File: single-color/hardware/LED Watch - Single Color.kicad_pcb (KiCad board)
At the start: 4 copper layers, 42 x 51.2 mm, 197 parts, among them J1 LiPo, J1B LiPo, J2 UPDI pogo pads 1.27 mm (RESET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, M0 LED white 0402, M1 LED white 0402, M10 LED white 0402, M11 LED white 0402, M12 LED white 0402, M13 LED white 0402, M14 LED white 0402, M15 LED white 0402, M16 LED white 0402, M17 LED white 0402, M18 LED white 0402, M19 LED white 0402, M2 LED white 0402, M20 LED white 0402, M21 LED white 0402, M22 LED white 0402, M23 LED white 0402, M24 LED white 0402, M25 LED white 0402, M26 LED white 0402, M27 LED white 0402, M28 LED white 0402, M29 LED white 0402, M3 LED white 0402, M30 LED white 0402, M31 LED white 0402, M32 LED white 0402, M33 LED white 0402, M34 LED white 0402, M35 LED white 0402, M36 LED white 0402, M37 LED white 0402, M38 LED white 0402, M39 LED white 0402, M4 LED white 0402, M40 LED white 0402, M41 LED white 0402, M42 LED white 0402, M43 LED white 0402, M44 LED white 0402, M45 LED white 0402, M46 LED white 0402, M47 LED white 0402, M48 LED white 0402, M49 LED white 0402, M5 LED white 0402, M50 LED white 0402, M51 LED white 0402, M52 LED white 0402, M53 LED white 0402, M54 LED white 0402, M55 LED white 0402, M56 LED white 0402, M57 LED white 0402, M58 LED white 0402, M59 LED white 0402, M6 LED white 0402, M7 LED white 0402, M8 LED white 0402, M9 LED white 0402, SW1 SW_Push, SW2 SW_Push, U1 AVR128DB48-I/6LX, U2 LIS2DW12TR, U4 BQ25570RGRR, Y1 32.768kHz

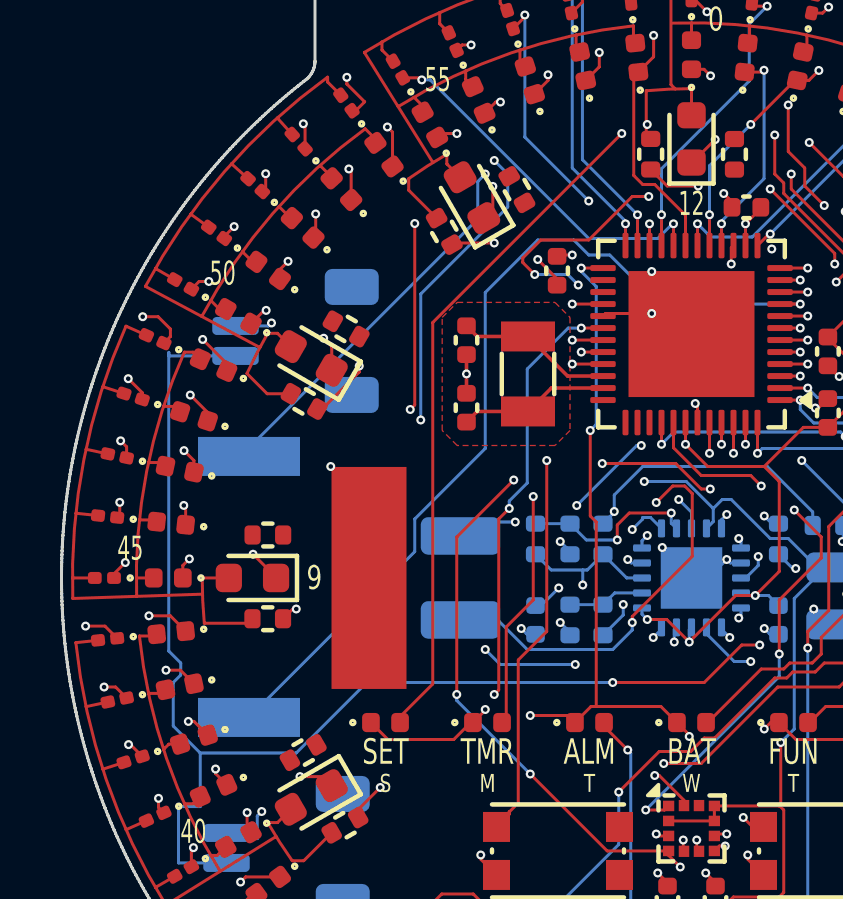
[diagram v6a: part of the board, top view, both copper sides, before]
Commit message: single-color: buzzer traces (BUZ_A, BUZ_B, COL1) moved out from under the battery plug by hand; gerbers re-exported
Co-Authored-By: Claude Sonnet 5.5 <noreply@anthropic.com>
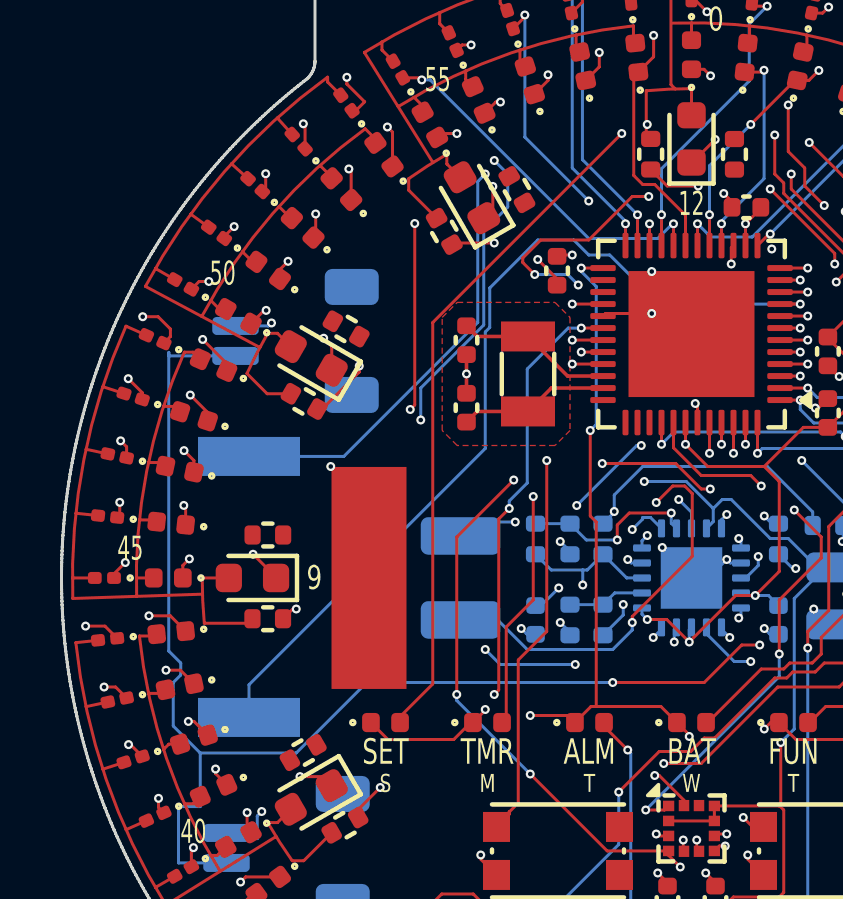
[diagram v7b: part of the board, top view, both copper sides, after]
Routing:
- net /BUZ_A: track 31.9 -> 33.8 mm
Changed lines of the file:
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@@
 	)
 	(segment
+		(start 93.075 91.567842)
+		(end 90.975 93.667842)
+		(width 0.1)
+		(layer "B.Cu")
+		(net "/COL1")
+	)
+	(segment
 		(start 93.875 87.635)
-		(end 90.975 90.535)
+		(end 93.075 88.435)
 		(width 0.1)
 		(layer "B.Cu")
@@
 	)
 	(segment
-		(start 90.975 90.535)
+		(start 93.875 86.535)
+		(end 93.875 87.635)
+		(width 0.1)
+		(layer "B.Cu")
+		(net "/COL1")
+	)
+	(segment
+		(start 90.975 93.667842)
 		(end 90.975 94.735)
 		(width 0.1)
@@
 	)
 	(segment
-		(start 93.875 86.535)
-		(end 93.875 87.635)
+		(start 93.075 88.435)
+		(end 93.075 91.567842)
 		(width 0.1)
 		(layer "B.Cu")
@@
 	)
 	(segment
-		(start 92.875 88.035)
-		(end 85.25 95.66)
+		(start 93.125 86.535)
+		(end 92.875 86.785)
 		(width 0.1)
 		(layer "B.Cu")
@@
 	)
 	(segment
-		(start 92.875 86.785)
-		(end 92.875 88.035)
+		(start 88.41 95.95)
+		(end 85.25 95.95)
 		(width 0.1)
 		(layer "B.Cu")
@@
 	)
 	(segment
-		(start 85.25 95.66)
-		(end 85.25 95.95)
+		(start 92.875 91.485)
+		(end 88.41 95.95)
 		(width 0.1)
 		(layer "B.Cu")
@@
 	)
 	(segment
-		(start 93.125 86.535)
-		(end 92.875 86.785)
+		(start 92.875 86.785)
+		(end 92.875 91.485)
 		(width 0.1)
 		(layer "B.Cu")
@@
 	)
 	(segment
-		(start 90.775 98.035)
-		(end 90.775 99.125)
+		(start 93.125 95.685)
+		(end 85.25 103.56)
 		(width 0.1)
 		(layer "B.Cu")
@@
 	)
 	(segment
-		(start 96.575 89.235)
-		(end 96.075 88.735)
+		(start 93.275 90.335)
+		(end 93.275 91.650684)
 		(width 0.1)
 		(layer "B.Cu")
@@
 	)
 	(segment
-		(start 97.275 89.235)
-		(end 96.575 89.235)
+		(start 93.275 91.650684)
+		(end 93.125 91.800684)
 		(width 0.1)
 		(layer "B.Cu")
@@
 	)
 	(segment
-		(start 90.775 99.125)
-		(end 85.25 104.65)
+		(start 94.875 88.735)
+		(end 93.275 90.335)
 		(width 0.1)
 		(layer "B.Cu")
@@
 	)
 	(segment
-		(start 96.075 88.735)
-		(end 94.875 88.735)
+		(start 103.625 90.87)
+		(end 98.91 90.87)
 		(width 0.1)
 		(layer "B.Cu")
@@
 	)
 	(segment
-		(start 103.625 90.87)
-		(end 98.91 90.87)
+		(start 93.125 91.800684)
+		(end 93.125 95.685)
 		(width 0.1)
 		(layer "B.Cu")
@@
 	)
 	(segment
-		(start 93.125 90.485)
-		(end 93.125 95.685)
+		(start 96.575 89.235)
+		(end 96.075 88.735)
 		(width 0.1)
 		(layer "B.Cu")
@@
 	)
 	(segment
-		(start 94.875 88.735)
-		(end 93.125 90.485)
+		(start 85.25 103.56)
+		(end 85.25 104.65)
 		(width 0.1)
 		(layer "B.Cu")
@@
 	)
 	(segment
-		(start 93.125 95.685)
-		(end 90.775 98.035)
+		(start 97.275 89.235)
+		(end 96.575 89.235)
+		(width 0.1)
+		(layer "B.Cu")
+		(net "/BUZ_B")
+	)
+	(segment
+		(start 96.075 88.735)
+		(end 94.875 88.735)
 		(width 0.1)
 		(layer "B.Cu")
